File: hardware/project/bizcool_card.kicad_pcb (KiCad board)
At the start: 4 copper layers, 85.6 x 53.9 mm, 145 parts, among them J1 XL-1005SURC, J2 Conn_01x03, SW1 SW_Push, SW2 SW_Push, U1 PRTR5V0U2X, U2 ME6211C33M5G, U3 ESP32-C3FN4, U4 W25Q128JVS

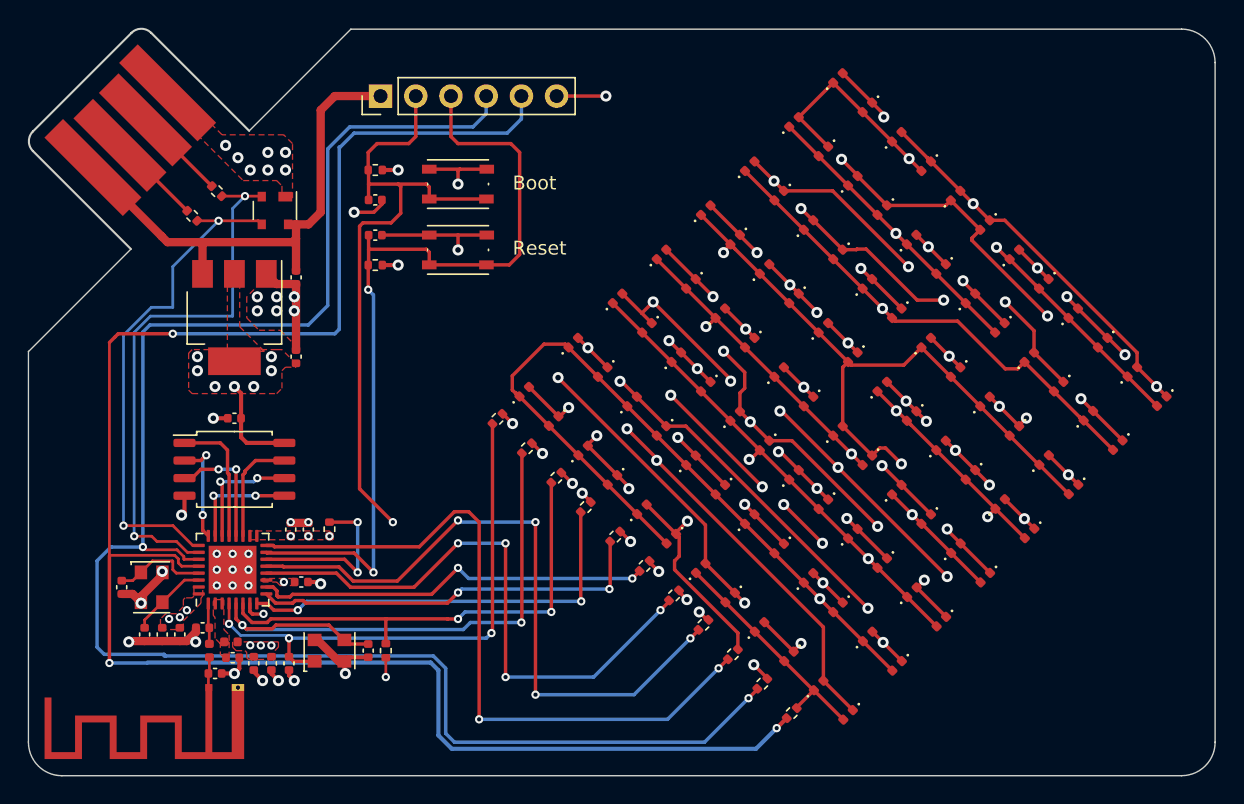
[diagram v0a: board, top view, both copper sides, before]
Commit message: move debug header out of the way
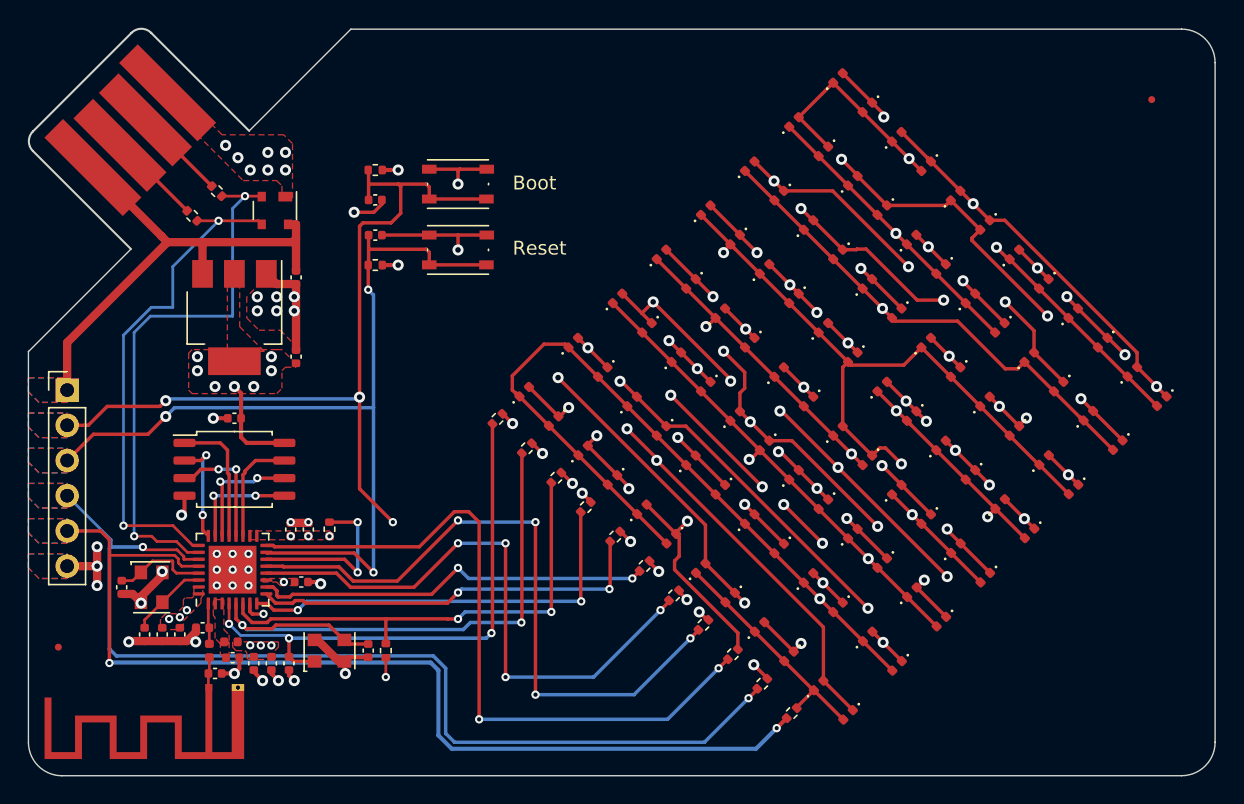
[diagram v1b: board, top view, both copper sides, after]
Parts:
- added REF1: Fiducial_0.5mm_Mask1mm, Fiducial:Fiducial_0.5mm_Mask1mm, F.Cu at (53.0, 95.4)
- added REF2: Fiducial_0.5mm_Mask1mm, Fiducial:Fiducial_0.5mm_Mask1mm, F.Cu at (131.8, 55.9)
- moved J2 31.0 mm to (53.6, 76.8), turned to 0 degrees
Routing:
- net /MX_R10: track 130.9 -> 74.3 mm, vias 3 -> 2
- net /MX_R9: track 124.1 -> 73.1 mm
- net /CHIP_RESET: track 63.4 -> 77.3 mm, vias 2 -> 4
- net /CHIP_BOOT: track 60.7 -> 66.0 mm, vias 2 -> 3
- net GND: track 52.9 -> 54.3 mm, vias 40 -> 42
- net /VUSB: track 37.4 -> 36.9 mm
- added copper zone on B.Cu, net (none)
- added copper zone on F.Cu, net (none)
- added copper zone on B.Cu, net /CHIP_BOOT
- added copper zone on F.Cu, net /CHIP_BOOT
- added copper zone on B.Cu, net /CHIP_RESET
- added copper zone on F.Cu, net /CHIP_RESET
- added copper zone on B.Cu, net /MX_R10
- added copper zone on F.Cu, net /MX_R10
- added copper zone on B.Cu, net /MX_R9
- added copper zone on F.Cu, net /MX_R9
- added copper zone on B.Cu, net /VUSB
- added copper zone on F.Cu, net /VUSB

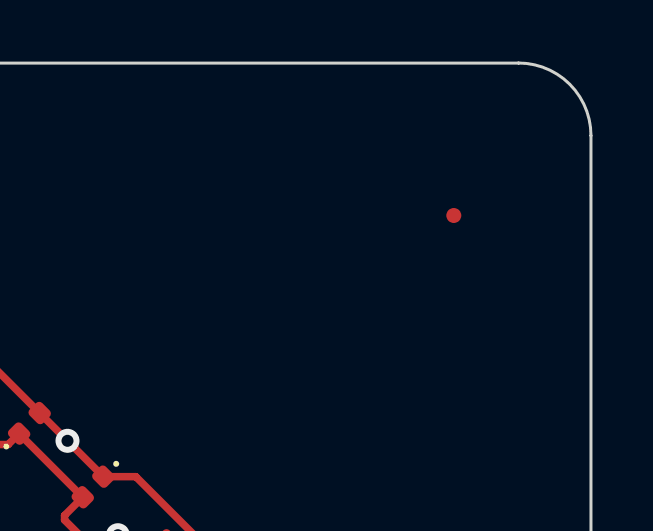
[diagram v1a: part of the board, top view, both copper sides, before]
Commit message: changed: script on the back face
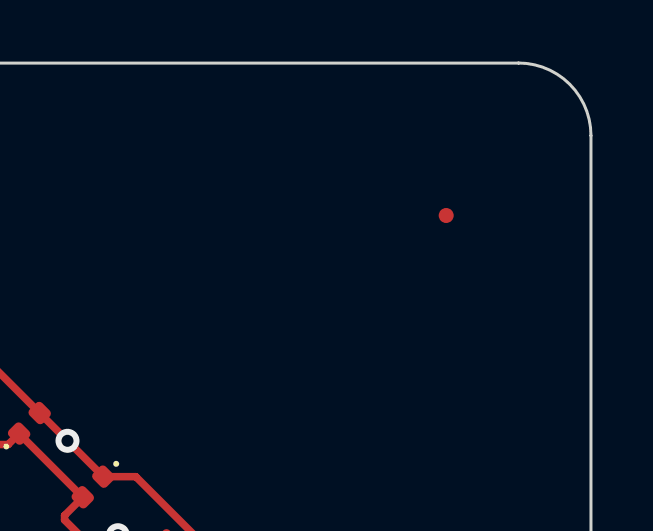
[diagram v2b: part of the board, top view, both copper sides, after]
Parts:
- moved REF2 0.25 mm to (131.6, 55.9)
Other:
- board text added: "A RISC-V gadget, with Python, Wi-Fi & Bluetooth. (Also, a business card)"
- board text removed: "(This business card runs Python)"
